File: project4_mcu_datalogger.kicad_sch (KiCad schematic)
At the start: 0 parts

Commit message: Setup of EEschema for new project
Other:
- title: (none) -> ${project_name}
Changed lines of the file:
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@@
 	(generator_version "9.0")
 	(paper "A4")
+	(title_block
+		(title "${project_name}")
+		(date "2025-12-01")
+		(rev "-")
+	)
 	(sheet_instances
 		(path "/"

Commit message: Have added required symbols to the schematic sheets
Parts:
- added BT1: Battery, symbol Device:Battery
- added C1, C2, C3, C4: C, symbol Device:C
- added C5: C_Polarized, symbol Device:C_Polarized
- added D1, D2: LED, symbol Device:LED
- added H1, H2, H3: MountingHole, symbol Mechanical:MountingHole
- added R1, R2, R3, R4, R5, R6, R7: R, symbol Device:R
- added U1, U2: 24LC1025, symbol Memory_EEPROM:24LC1025
- added U3: ATMEGA328P-AU, ATMEGA328P-AU:QFP80P900X900X120-32N, symbol ATMEGA328P-AU:ATMEGA328P-AU
- added U4: DS1337S_T_R, DS1337S_T_R:SOIC127P600X175-8N, symbol DS1337S_T_R:DS1337S_T_R
- added Y1, Y2: Crystal, symbol Device:Crystal
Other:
- added sheet Connectors (connectors.kicad_sch)

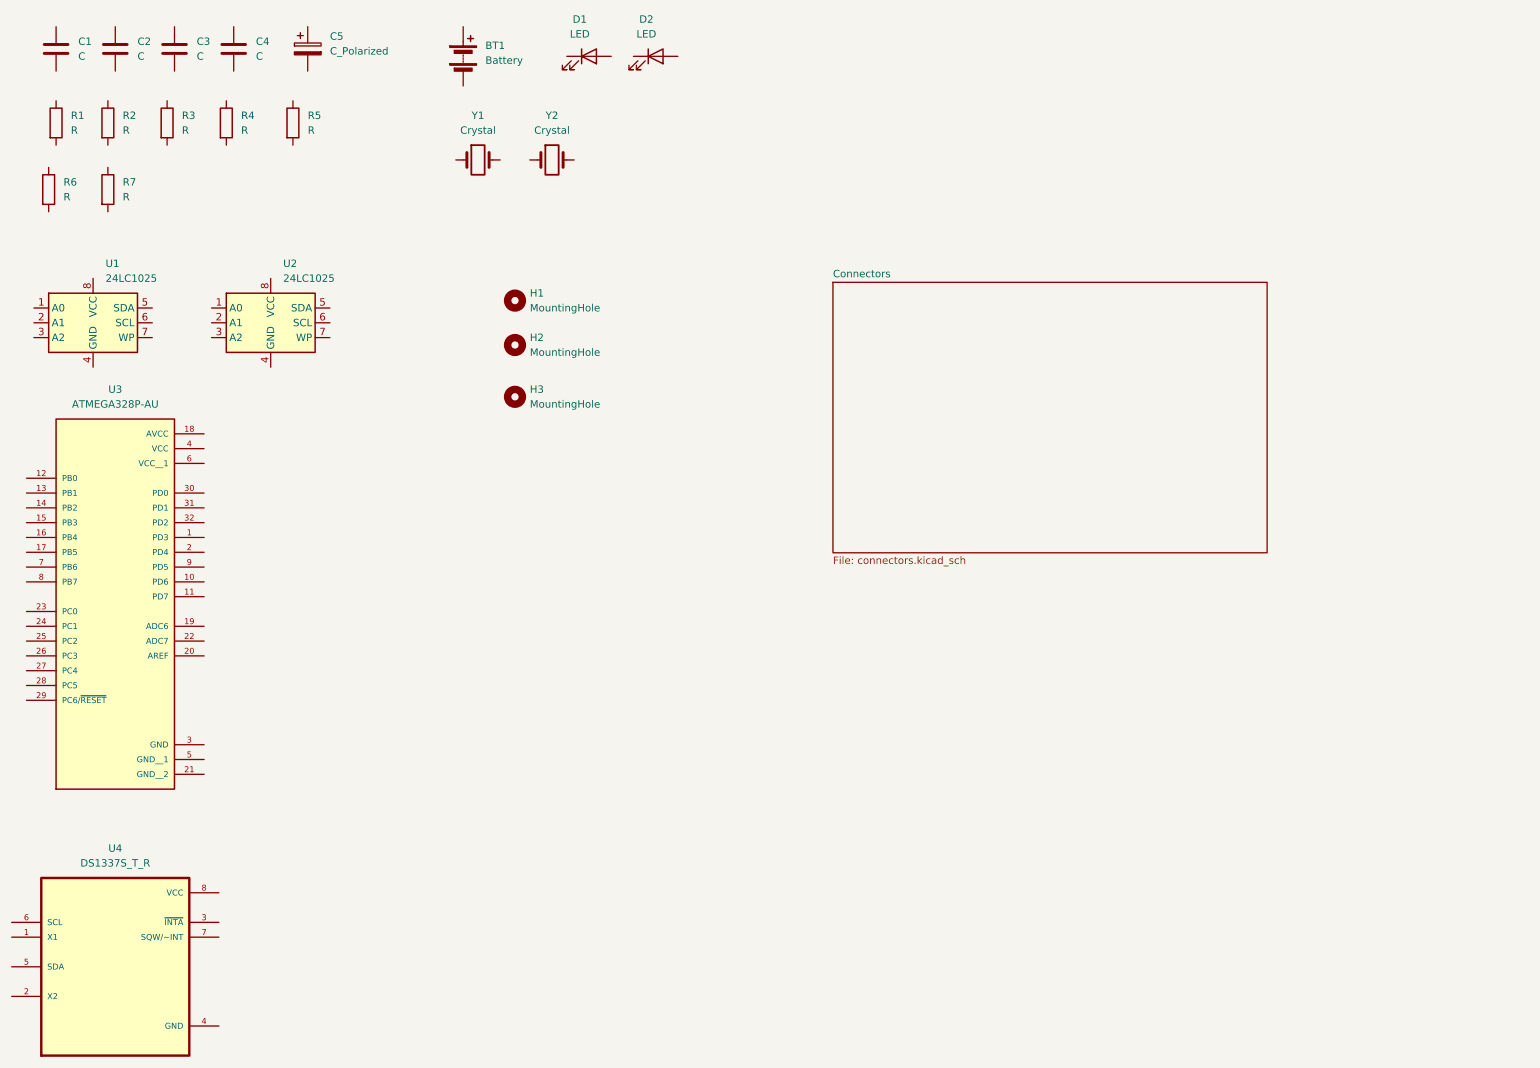
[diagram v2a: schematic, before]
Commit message: Changed locations of symbols
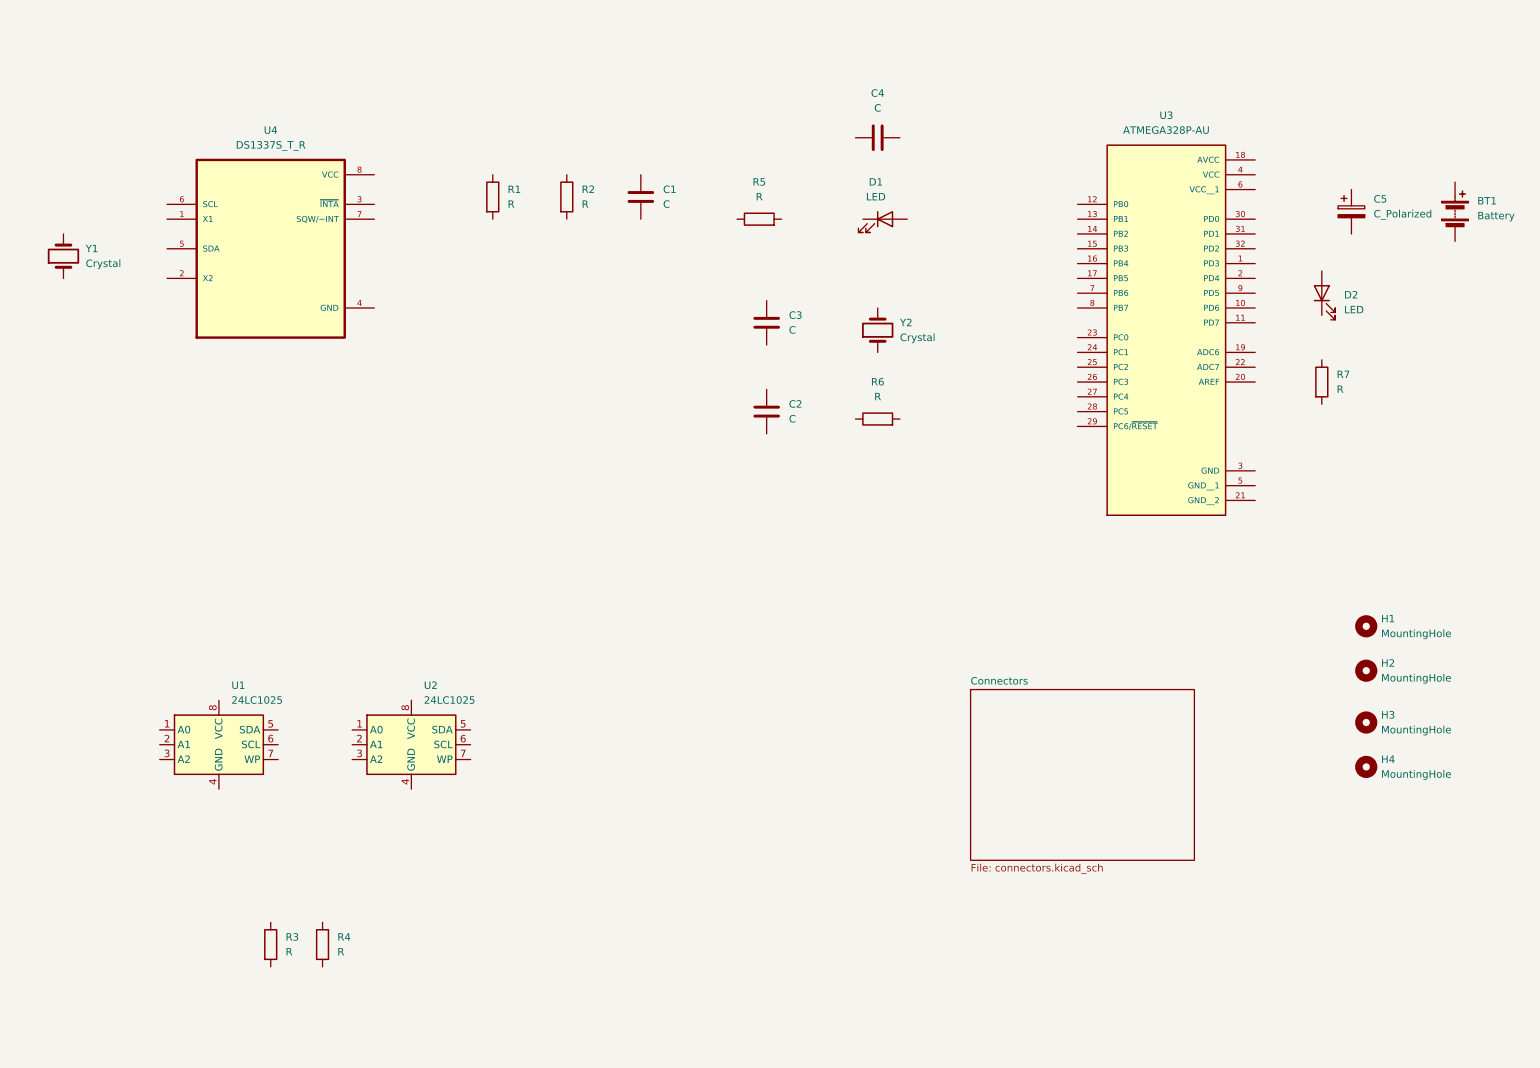
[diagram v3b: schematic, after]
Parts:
- added H4: MountingHole, symbol Mechanical:MountingHole
- renumbered R3 to R1, R4 to R2, R1 to R3, R2 to R4, R6 to R5, R5 to R6
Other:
- moved on the sheet: BT1, C1, C2, C3, C4, C5, D1, D2, H1, H2, H3, R1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

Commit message: Added component values
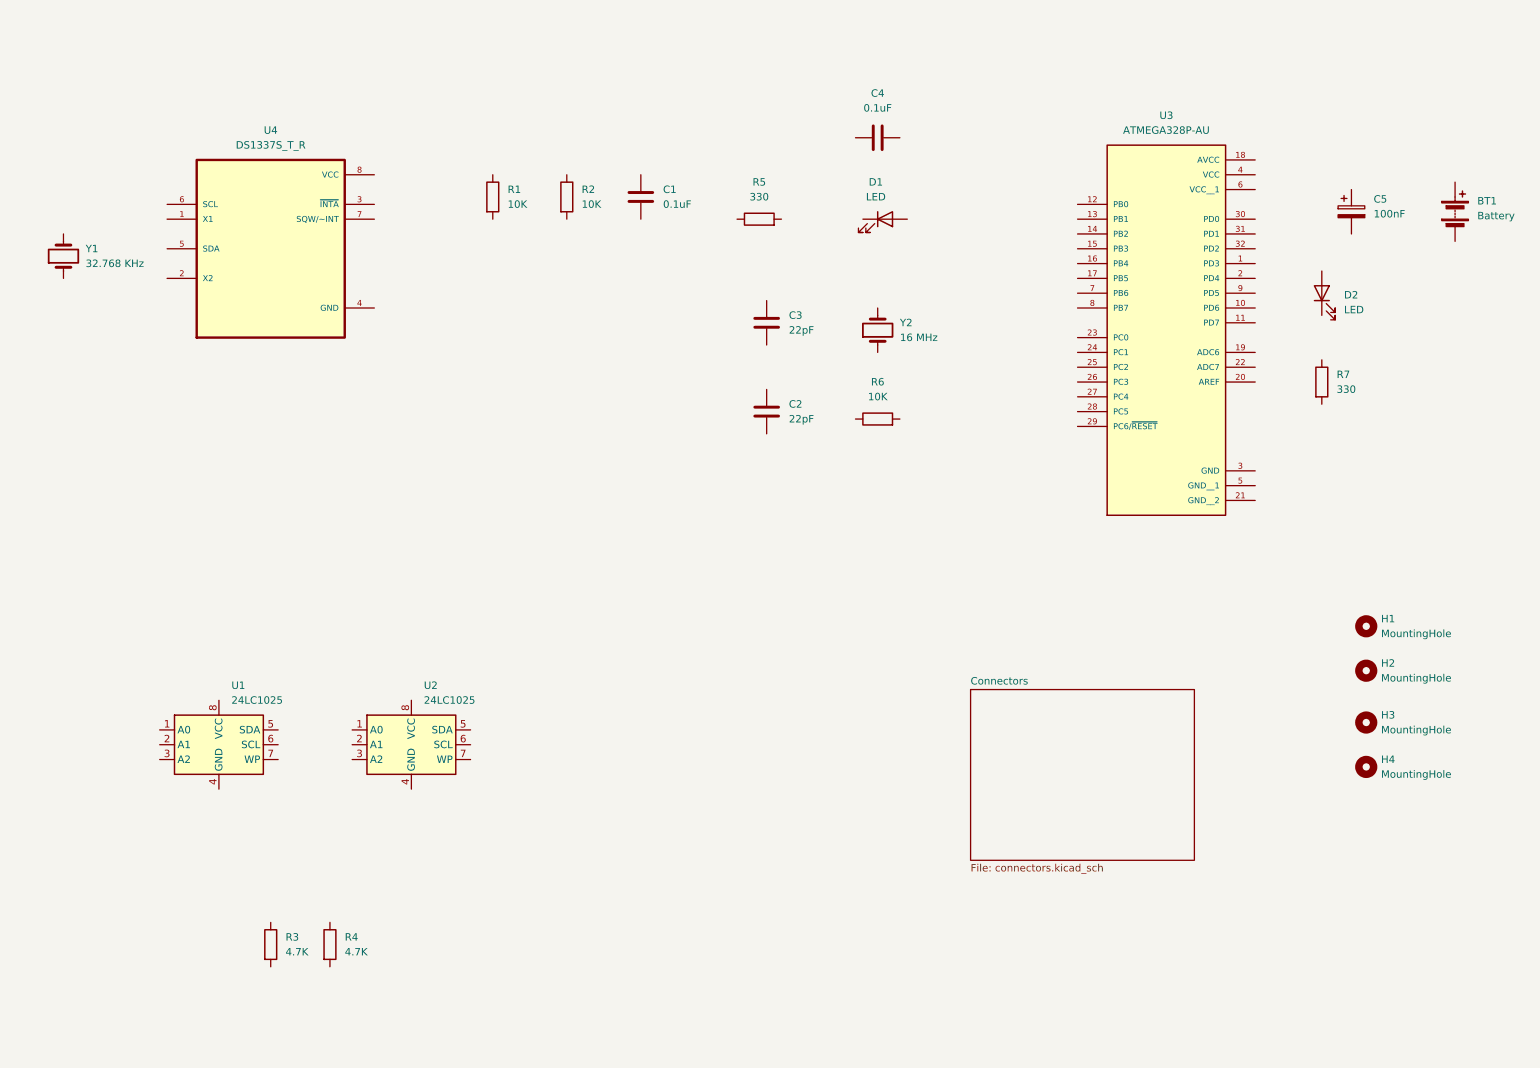
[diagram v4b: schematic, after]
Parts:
- C1, C4: value C -> 0.1uF
- C2, C3: value C -> 22pF
- C5: value C_Polarized -> 100nF
- R1, R2, R6: value R -> 10K
- R3, R4: value R -> 4.7K
- R5, R7: value R -> 330
- Y1: value Crystal -> 32.768 KHz
- Y2: value Crystal -> 16 MHz
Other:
- moved on the sheet: R4
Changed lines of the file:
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@@
 			)
 		)
-		(property "Value" "R"
+		(property "Value" "330"
 			(at 243.84 80.0099 0)
 			(effects
@@
 			)
 		)
-		(property "Value" "C"
+		(property "Value" "0.1uF"
 			(at 128.27 48.2599 0)
 			(effects
@@
 			)
 		)
-		(property "Value" "R"
+		(property "Value" "330"
 			(at 144.78 46.99 90)
 			(effects
@@
 			)
 		)
-		(property "Value" "C"
+		(property "Value" "22pF"
 			(at 149.86 85.0899 0)
 			(effects
@@
 			)
 		)
-		(property "Value" "C"
+		(property "Value" "0.1uF"
 			(at 165.1 31.75 90)
 			(effects
@@
 	(symbol
 		(lib_id "Device:R")
-		(at 69.85 175.26 0)
+		(at 71.12 175.26 0)
 		(unit 1)
 		(exclude_from_sim no)
@@
 		(fields_autoplaced yes)
 		(property "Reference" "R4"
-			(at 72.39 173.9899 0)
-			(effects
-				(font
-					(size 1.27 1.27)
-				)
-				(justify left)
-			)
-		)
-		(property "Value" "R"
-			(at 72.39 176.5299 0)
-			(effects
-				(font
-					(size 1.27 1.27)
-				)
-				(justify left)
-			)
-		)
-		(property "Footprint" ""
-			(at 68.072 175.26 90)
-			(effects
-				(font
-					(size 1.27 1.27)
-				)
-				(hide yes)
-			)
-		)
-		(property "Datasheet" "~"
-			(at 69.85 175.26 0)
+			(at 73.66 173.9899 0)
+			(effects
+				(font
+					(size 1.27 1.27)
+				)
+				(justify left)
+			)
+		)
+		(property "Value" "4.7K"
+			(at 73.66 176.5299 0)
+			(effects
+				(font
+					(size 1.27 1.27)
+				)
+				(justify left)
+			)
+		)
+		(property "Footprint" ""
+			(at 69.342 175.26 90)
+			(effects
+				(font
+					(size 1.27 1.27)
+				)
+				(hide yes)
+			)
+		)
+		(property "Datasheet" "~"
+			(at 71.12 175.26 0)
 			(effects
 				(font
@@
 		)
 		(property "Description" "Resistor"
-			(at 69.85 175.26 0)
+			(at 71.12 175.26 0)
 			(effects
 				(font
@@
 			)
 		)
-		(property "Value" "C"
+		(property "Value" "22pF"
 			(at 149.86 69.8499 0)
 			(effects
@@
 			)
 		)
-		(property "Value" "C_Polarized"
+		(property "Value" "100nF"
 			(at 250.19 49.9109 0)
 			(effects
@@
 			)
 		)
-		(property "Value" "Crystal"
+		(property "Value" "16 MHz"
 			(at 168.91 71.1199 90)
 			(effects
@@
 			)
 		)
-		(property "Value" "Crystal"
+		(property "Value" "32.768 KHz"
 			(at 29.21 58.4199 90)
 			(effects
@@
 			)
 		)
-		(property "Value" "R"
+		(property "Value" "10K"
 			(at 101.6 48.2599 0)
 			(effects
@@
 			)
 		)
-		(property "Value" "R"
+		(property "Value" "10K"
 			(at 114.3 48.2599 0)
 			(effects
@@
 			)
 		)
-		(property "Value" "R"
+		(property "Value" "10K"
 			(at 165.1 81.28 90)
 			(effects
@@
 			)
 		)
-		(property "Value" "R"
+		(property "Value" "4.7K"
 			(at 63.5 176.5299 0)
 			(effects

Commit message: Completed symbol to footprint associations
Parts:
- BT1: footprint (none) -> Connector_PinHeader_2.54mm:PinHeader_1x02_P2.54mm_Vertical
- C1, C2, C3, C4, C5: footprint (none) -> Capacitor_SMD:C_0805_2012Metric
- D1, D2: footprint (none) -> LED_SMD:LED_0805_2012Metric
- H1, H2, H3, H4: footprint (none) -> MountingHole:MountingHole_2.1mm
- R1, R2, R3, R4, R5, R6, R7: footprint (none) -> Resistor_SMD:R_0805_2012Metric
- U1, U2: footprint (none) -> Package_SO:SOIC-8_5.3x5.3mm_P1.27mm
- U3: footprint ATMEGA328P-AU:QFP80P900X900X120-32N -> ATMEGA328P_AU:QFP80P900X900X120-32N
- Y1, Y2: footprint (none) -> Crystal:Crystal_SMD_Abracon_ABM3-2Pin_5.0x3.2mm_HandSoldering
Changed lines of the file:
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@@
 			)
 		)
-		(property "Footprint" ""
+		(property "Footprint" "Resistor_SMD:R_0805_2012Metric"
 			(at 239.522 78.74 90)
 			(effects
@@
 			)
 		)
-		(property "Footprint" ""
+		(property "Footprint" "MountingHole:MountingHole_2.1mm"
 			(at 248.92 144.78 0)
 			(effects
@@
 			)
 		)
-		(property "Footprint" ""
+		(property "Footprint" "Capacitor_SMD:C_0805_2012Metric"
 			(at 125.4252 50.8 0)
 			(effects
@@
 			)
 		)
-		(property "Footprint" ""
+		(property "Footprint" "Resistor_SMD:R_0805_2012Metric"
 			(at 144.78 52.578 90)
 			(effects
@@
 			)
 		)
-		(property "Footprint" ""
+		(property "Footprint" "Connector_PinHeader_2.54mm:PinHeader_1x02_P2.54mm_Vertical"
 			(at 264.16 48.006 90)
 			(effects
@@
 			)
 		)
-		(property "Footprint" ""
+		(property "Footprint" "Capacitor_SMD:C_0805_2012Metric"
 			(at 147.0152 87.63 0)
 			(effects
@@
 			)
 		)
-		(property "Footprint" ""
+		(property "Footprint" "MountingHole:MountingHole_2.1mm"
 			(at 248.92 128.27 0)
 			(effects
@@
 			)
 		)
-		(property "Footprint" ""
+		(property "Footprint" "Capacitor_SMD:C_0805_2012Metric"
 			(at 168.91 35.8648 0)
 			(effects
@@
 			)
 		)
-		(property "Footprint" ""
+		(property "Footprint" "Resistor_SMD:R_0805_2012Metric"
 			(at 69.342 175.26 90)
 			(effects
@@
 			)
 		)
-		(property "Footprint" ""
+		(property "Footprint" "Capacitor_SMD:C_0805_2012Metric"
 			(at 147.0152 72.39 0)
 			(effects
@@
 			)
 		)
-		(property "Footprint" ""
+		(property "Footprint" "Package_SO:SOIC-8_5.3x5.3mm_P1.27mm"
 			(at 52.07 140.97 0)
 			(effects
@@
 			)
 		)
-		(property "Footprint" ""
+		(property "Footprint" "MountingHole:MountingHole_2.1mm"
 			(at 248.92 137.16 0)
 			(effects
@@
 			)
 		)
-		(property "Footprint" ""
+		(property "Footprint" "LED_SMD:LED_0805_2012Metric"
 			(at 166.37 50.8 0)
 			(effects
@@
 			)
 		)
-		(property "Footprint" ""
+		(property "Footprint" "MountingHole:MountingHole_2.1mm"
 			(at 248.92 120.65 0)
 			(effects
@@
 			)
 		)
-		(property "Footprint" ""
+		(property "Footprint" "Capacitor_SMD:C_0805_2012Metric"
 			(at 247.3452 53.34 0)
 			(effects
@@
 			)
 		)
-		(property "Footprint" ""
+		(property "Footprint" "LED_SMD:LED_0805_2012Metric"
 			(at 241.3 63.5 0)
 			(effects
@@
 			)
 		)
-		(property "Footprint" ""
+		(property "Footprint" "Crystal:Crystal_SMD_Abracon_ABM3-2Pin_5.0x3.2mm_HandSoldering"
 			(at 165.1 69.85 0)
 			(effects
@@
 			)
 		)
-		(property "Footprint" ""
+		(property "Footprint" "Crystal:Crystal_SMD_Abracon_ABM3-2Pin_5.0x3.2mm_HandSoldering"
 			(at 25.4 57.15 0)
 			(effects
@@
 			)
 		)
-		(property "Footprint" ""
+		(property "Footprint" "Package_SO:SOIC-8_5.3x5.3mm_P1.27mm"
 			(at 85.09 140.97 0)
 			(effects
@@
 			)
 		)
-		(property "Footprint" ""
+		(property "Footprint" "Resistor_SMD:R_0805_2012Metric"
 			(at 97.282 46.99 90)
 			(effects
@@
 			)
 		)
-		(property "Footprint" ""
+		(property "Footprint" "Resistor_SMD:R_0805_2012Metric"
 			(at 109.982 46.99 90)
 			(effects
@@
 			)
 		)
-		(property "Footprint" ""
+		(property "Footprint" "Resistor_SMD:R_0805_2012Metric"
 			(at 165.1 86.868 90)
 			(effects
@@
 			)
 		)
-		(property "Footprint" "ATMEGA328P-AU:QFP80P900X900X120-32N"
+		(property "Footprint" "ATMEGA328P_AU:QFP80P900X900X120-32N"
 			(at 214.63 66.04 0)
 			(effects
@@
 			)
 		)
-		(property "Footprint" ""
+		(property "Footprint" "Resistor_SMD:R_0805_2012Metric"
 			(at 59.182 175.26 90)
 			(effects
